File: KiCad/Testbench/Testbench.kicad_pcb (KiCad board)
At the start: 2 copper layers, 119 parts, among them J1 Conn_02x03_Counter_Clockwise, J10 Conn_01x02_Pin, J11 Conn_01x02_Pin, J12 Conn_01x02_Pin, J13 Conn_01x02_Pin, J14 Conn_01x02_Pin, J15 Conn_01x02_Pin, J16 Conn_01x02_Pin, J17 Conn_01x02_Pin, J18 Conn_02x03_Counter_Clockwise, J19 Conn_02x03_Counter_Clockwise, J2 Conn_02x02_Top_Bottom, J20 Conn_02x05_Top_Bottom, J21 Conn_02x02_Top_Bottom, J3 Conn_02x02_Top_Bottom, J4 Conn_02x02_Top_Bottom, J5 Conn_01x01_Pin, J6 Conn_02x05_Counter_Clockwise, J7 Conn_01x02_Pin, J8 Conn_01x02_Pin, J9 Conn_02x05_Counter_Clockwise

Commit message: PCB before first processing
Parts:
- removed the D20 at (111.1, 29.6)
- removed the D21 at (52.2, 62.0)
- removed the D22 at (65.3, 32.4)
- removed the D5 at (139.7, 137.9)
- removed the D6 at (139.8, 144.9)
- removed J5: Conn_01x01_Pin, Connector_Molex:Molex_Mini-Fit_Jr_5566-04A_2x02_P4.20mm_Vertical
- removed the R22 at (111.1, 34.8)
- removed the R23 at (52.2, 57.0)
- removed the R24 at (115.5, 29.4)
- removed R30: R100k, Resistor_SMD:R_1206_3216Metric_Pad1.30x1.75mm_HandSolder
- removed R31: R300, Resistor_SMD:R_1206_3216Metric_Pad1.30x1.75mm_HandSolder
- removed the R6 at (134.8, 102.5)
- removed the R7 at (134.3, 137.9)
- removed the R8 at (134.1, 144.9)
- removed TP44: TestPoint, TestPoint:TestPoint_Keystone_5010-5014_Multipurpose
- added D1: LED, LED_SMD:LED_0805_2012Metric_Pad1.15x1.40mm_HandSolder, B.Cu at (88.1, 67.8)
- added D14: LED, LED_SMD:LED_0805_2012Metric_Pad1.15x1.40mm_HandSolder, B.Cu at (126.7, 105.0)
- added D15: LED, LED_SMD:LED_0805_2012Metric_Pad1.15x1.40mm_HandSolder, B.Cu at (126.5, 145.0)
- added D16: LED, LED_SMD:LED_0805_2012Metric_Pad1.15x1.40mm_HandSolder, B.Cu at (126.7, 95.0)
- added D25: LED, LED_SMD:LED_0805_2012Metric_Pad1.15x1.40mm_HandSolder, B.Cu at (204.8, 33.3)
- added D26: LED, LED_SMD:LED_0805_2012Metric_Pad1.15x1.40mm_HandSolder, B.Cu at (81.5, 35.7)
- added D27: LED, LED_SMD:LED_0805_2012Metric_Pad1.15x1.40mm_HandSolder, B.Cu at (124.3, 35.8)
- added D3: LED, LED_SMD:LED_0805_2012Metric_Pad1.15x1.40mm_HandSolder, B.Cu at (88.3, 75.3)
- added J21: Conn_02x02_Top_Bottom, Connector_Molex:Molex_Mini-Fit_Jr_5566-04A_2x02_P4.20mm_Vertical, F.Cu at (156.6, 46.2)
- added J22: Conn_02x02_Top_Bottom, Connector_Molex:Molex_Mini-Fit_Jr_5566-04A_2x02_P4.20mm_Vertical, F.Cu at (22.7, 48.8)
- added J23: Conn_02x02_Top_Bottom, Connector_Molex:Molex_Mini-Fit_Jr_5566-04A_2x02_P4.20mm_Vertical, F.Cu at (195.7, 45.8)
- added J24: Conn_02x02_Top_Bottom, Connector_Molex:Molex_Mini-Fit_Jr_5566-04A_2x02_P4.20mm_Vertical, F.Cu at (69.5, 21.8)
- added J25: Conn_02x02_Top_Bottom, Connector_Molex:Molex_Mini-Fit_Jr_5566-04A_2x02_P4.20mm_Vertical, F.Cu at (195.7, 21.8)
- added J26: Conn_02x02_Top_Bottom, Connector_Molex:Molex_Mini-Fit_Jr_5566-04A_2x02_P4.20mm_Vertical, F.Cu at (69.5, 48.5)
- added J27: Conn_02x02_Top_Bottom, Connector_Molex:Molex_Mini-Fit_Jr_5566-04A_2x02_P4.20mm_Vertical, F.Cu at (113.2, 21.5)
- added J28: Conn_02x02_Top_Bottom, Connector_Molex:Molex_Mini-Fit_Jr_5566-04A_2x02_P4.20mm_Vertical, F.Cu at (113.3, 46.8)
- added R1: R1k1, Resistor_SMD:R_1206_3216Metric_Pad1.30x1.75mm_HandSolder, B.Cu at (83.3, 67.8)
- added R16: R1k1, Resistor_SMD:R_1206_3216Metric_Pad1.30x1.75mm_HandSolder, B.Cu at (131.4, 105.0)
- added R17: R1k1, Resistor_SMD:R_1206_3216Metric_Pad1.30x1.75mm_HandSolder, B.Cu at (131.3, 145.0)
- added R18: R1k1, Resistor_SMD:R_1206_3216Metric_Pad1.30x1.75mm_HandSolder, B.Cu at (131.4, 95.0)
- added R3: R1k1, Resistor_SMD:R_1206_3216Metric_Pad1.30x1.75mm_HandSolder, B.Cu at (83.5, 75.3)
- added R4: R1k1, Resistor_SMD:R_1206_3216Metric_Pad1.30x1.75mm_HandSolder, B.Cu at (83.6, 79.1)
- D10, D11, D12, D13, D23, D24, D4, D7, D8, D9, R10, R11, R12, R13, R14, R15, R26, R29, R9: moved to B.Cu
- D17: renamed from D14; moved to B.Cu
- D18: renamed from D15; moved to B.Cu
- D19: renamed from D16; moved to B.Cu
- D2: renamed from D1; moved to B.Cu
- D20: renamed from D17; moved to B.Cu
- D21: renamed from D18; moved to B.Cu
- D22: renamed from D19; moved to B.Cu
- D5: renamed from D2; moved to B.Cu
- D6: renamed from D3; moved to B.Cu
- J1: footprint Connector_Molex:Molex_Mini-Fit_Jr_5566-06A_2x03_P4.20mm_Vertical -> Connector_Molex:Molex_Mini-Fit_Jr_5566-08A_2x04_P4.20mm_Vertical
- J19: value Conn_02x03_Counter_Clockwise -> Conn_02x02_Top_Bottom; footprint Connector_Molex:Molex_Mini-Fit_Jr_5566-06A_2x03_P4.20mm_Vertical -> Connector_Molex:Molex_Mini-Fit_Jr_5566-04A_2x02_P4.20mm_Vertical
- J20: value Conn_02x05_Top_Bottom -> Conn_02x02_Top_Bottom; footprint Connector_Molex:Molex_Mini-Fit_Jr_5566-10A_2x05_P4.20mm_Vertical -> Connector_Molex:Molex_Mini-Fit_Jr_5566-04A_2x02_P4.20mm_Vertical
- R19: renamed from R16; moved to B.Cu
- R2: renamed from R1; moved to B.Cu
- R20: renamed from R17; moved to B.Cu
- R21: renamed from R18; moved to B.Cu
- R22: renamed from R19; moved to B.Cu
- R23: renamed from R20; moved to B.Cu
- R24: renamed from R21; moved to B.Cu
- R25, R27, R28: value R100k -> R300; moved to B.Cu
- R5: renamed from R2; moved to B.Cu
- R6: renamed from R3; moved to B.Cu
- R7: renamed from R4; moved to B.Cu
- R8: renamed from R5; moved to B.Cu
- moved J3 166.3 mm to (23.1, 105.5)
- moved J4 154.3 mm to (22.6, 87.5)
- moved D17 146.2 mm to (199.9, 77.5)
- moved R19 146.2 mm to (195.3, 77.5)
- moved D20 146.1 mm to (199.8, 82.0)
- moved R22 146.1 mm to (195.3, 82.0), turned to 0 degrees
- moved R24 146.0 mm to (195.1, 73.5)
- moved D22 146.0 mm to (199.8, 73.5)
- moved TP1 144.5 mm to (34.3, 105.5)
- moved TP3 144.2 mm to (34.3, 111.0)
- moved R7 143.1 mm to (41.3, 108.5)
- moved J18 137.1 mm to (171.6, 81.9)
- moved TP4 130.6 mm to (33.8, 87.5)
- moved TP5 130.5 mm to (33.8, 93.0)
- moved R8 129.4 mm to (40.8, 90.5)
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- renumbered J21 to J29
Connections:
- D10 pad 2: /Shutdown Circuit/1-C4 -> /Shutdown Circuit/1-A1
- D11 pad 2: /Shutdown Circuit/1-E2 -> /Shutdown Circuit/1-B2
- D12 pad 2: /Shutdown Circuit/1-C2 -> /Shutdown Circuit/1-D4
- D13 pad 2: /Shutdown Circuit/1-F1 -> /Shutdown Circuit/1-B4
- D23 pad 1: /Sensors/3-A3 -> /Sensors/3-A2
- D24 pad 1: /Sensors/3-C3 -> /Sensors/2-M4
- D4 pad 1: Net-(D4-K) -> GND-LV_Unfiltered
- D4 pad 2: /Shutdown Circuit/1-A2 -> Net-(D4-A)
- D7 pad 2: /Shutdown Circuit/1-B1 -> /Shutdown Circuit/1-A3
- D8 pad 2: /Shutdown Circuit/1-B3 -> /Shutdown Circuit/1-C1
- D9 pad 2: /Shutdown Circuit/1-E4 -> /Shutdown Circuit/1-D2
- J1 pad 1: /Actuators/2-B4 -> /Actuators/1-G3
- J1 pad 2: /Actuators/2-E4 -> /Actuators/2-C4
- J1 pad 3: /Actuators/1-G3 -> /Actuators/2-D4
- J1 pad 4: GND-LV_Unfiltered -> /Actuators/1-G4
- J1 pad 5: /Actuators/1-G3 -> /Actuators/2-E4
- J1 pad 6: /Actuators/1-G3 -> /Actuators/2-B4
- J19 pad 1: /Sensors/3-A1 -> /Sensors/2-M2
- J19 pad 2: /Sensors/3-B1 -> /Sensors/2-M4
- J19 pad 3: /Sensors/3-A2 -> unconnected-(J19-Pin_3-Pad3)
- J19 pad 4: /Sensors/3-A3 -> /Sensors/2-M3
- J20 pad 1: /Sensors/3-B4 -> /Sensors/3-A1
- J20 pad 2: /Sensors/3-C1 -> /Sensors/3-A2
- J20 pad 3: /Sensors/3-B3 -> unconnected-(J20-Pin_3-Pad3)
- J20 pad 4: /Sensors/2-M2 -> /Sensors/3-B1
- J29 pad 3: unconnected-(J21-Pin_3-Pad3) -> +24V
- J29 pad 4: GND -> GND-LV_Unfiltered
- R2 pad 1: /Actuators/1-G3 -> /Actuators/2-C4
- R25 pad 1: /Sensors/2-M3 -> /Sensors/3-A1
- R25 pad 2: /Sensors/2-M4 -> Net-(D23-A)
- R26 pad 1: /Sensors/3-B4 -> /Sensors/2-M2
- R26 pad 2: Net-(D22-A) (its old number) -> Net-(D24-A)
- R27 pad 1: /Sensors/3-B2 -> /Sensors/3-A4
- R27 pad 2: /Sensors/3-A3 -> Net-(D25-A)
- R28 pad 1: /Sensors/3-C1 -> /Sensors/3-B4
- R28 pad 2: /Sensors/3-B3 -> Net-(D26-A)
- R29 pad 1: /Sensors/3-A4 -> /Sensors/3-C4
- R29 pad 2: Net-(D23-A) -> Net-(D27-A)
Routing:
- net /Shutdown Circuit/1-E1: track 0.00 -> 127.9 mm, vias 0 -> 1
- net /Shutdown Circuit/1-E3: track 0.00 -> 110.9 mm, vias 0 -> 1
- net /Shutdown Circuit/1-D4: track 0.00 -> 94.5 mm, vias 0 -> 1
- net /Shutdown Circuit/1-D2: track 0.00 -> 78.4 mm, vias 0 -> 1
- net /Sensors/3-B4: track 14.8 -> 88.0 mm, vias 0 -> 1
- net /Shutdown Circuit/1-A3: track 5.99 -> 78.3 mm, vias 0 -> 1
- net /Shutdown Circuit/1-A1: track 0.00 -> 69.5 mm, vias 0 -> 1
- net /Sensors/3-A4: track 9.69 -> 73.6 mm, vias 0 -> 1
- net /Shutdown Circuit/1-B2: track 0.00 -> 63.2 mm, vias 0 -> 1
- net /Shutdown Circuit/1-C1: track 0.00 -> 63.0 mm, vias 0 -> 1
- net /Sensors/3-C4: track 15.7 -> 78.7 mm, vias 0 -> 1
- net /Sensors/2-M2: track 24.9 -> 87.6 mm, vias 0 -> 1
- net /Shutdown Circuit/1-B4: track 0.00 -> 61.2 mm, vias 0 -> 1
- net +24V: track 80.6 -> 20.2 mm
- net /Shutdown Circuit/1-C3: track 0.00 -> 58.8 mm, vias 0 -> 1
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- added copper zone on F.Cu, net (none)
- added copper zone on B.Cu, net GND-LV_Unfiltered
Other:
- board outline added: 224 x 186 mm
- board text added: "Actuators"
- board text added: "BP0_SUP"
- board text added: "Brake Pressure 0 (BP0)"
- board text added: "Brake Pressure 0 (BP1)"
- board text added: "Brake Pressure 1 (BP1)"
- board text added: "CAN GND FILTERED GND"
- board text added: "COOLING 1-G3"
- board text added: "COOLING 1-G4"
- board text added: "COOLING 2-C4"
- board text added: "COOLING 2-D4"
- board text added: "External Power"
- board text added: "Inputs"
- board text added: "Mangler: Forket side skal laves på bagsiden Og så skal der laves om på SDC. Sensorkreds. Tjek om forsyning er der. Monter huller til ben."
- board text added: "Outputs"
- board text added: "Power 24VDC"
- board text added: "Power Distribution"
- board text added: "SC.._IN SIGNALS"
- board text added: "SC.._OUT SIGNALS"
- board text added: "SC_BOTS_IN"
- board text added: "SC_Cockpit_IN"
- board text added: "SC_FL_IN"
- board text added: "SC_FR_IN"
- board text added: "SC_Inertia_IN"
- board text added: "SC_Left_IN"
- board text added: "SC_RL_IN"
- board text added: "SC_RR_IN"
- board text added: "SC_Right_IN"
- board text added: "SC_TSMS_IN"
- board text added: "Shutdown Circuit (SDC)"
- board text added: "Steering Wheel"
- board text added: "Unfiltered GND"
- board text removed: "BP0_SUPPLY"
- board text removed: "COOLING"
- board text removed: "GND"
- board text removed: "Mangler: Forket side skal laves på bagsiden Og så skal der laves om på SDC."
- board text removed: "TP1_GND"
- board text removed: "TP1_SIG"
- board text removed: "TP1_SUP"

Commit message: After work 151024
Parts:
- moved R7 38.0 mm to (42.0, 146.6)
- moved R8 38.0 mm to (41.5, 128.6)
- moved J2 38.0 mm to (23.3, 107.5)
- moved J3 38.0 mm to (23.8, 143.5)
- moved J4 38.0 mm to (23.3, 125.5)
- moved TP1 38.0 mm to (35.0, 143.5)
- moved TP2 38.0 mm to (36.5, 107.0)
- moved TP3 38.0 mm to (35.0, 149.0)
- moved TP4 38.0 mm to (34.5, 125.5)
- moved TP5 38.0 mm to (34.5, 131.0)
- moved D17 33.9 mm to (166.6, 70.8)
- moved D18 33.9 mm to (114.7, 75.8)
- moved D19 33.9 mm to (114.8, 70.8)
- moved D21 33.9 mm to (115.0, 65.8)
- moved D22 33.9 mm to (166.5, 66.8)
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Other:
- board size 224 x 186 mm -> 204.2 x 186.5 mm
- board text added: "Steering Wheel (SW)"
- board text removed: "Brake Pressure 0 (BP1)"
- board text removed: "Steering Wheel"

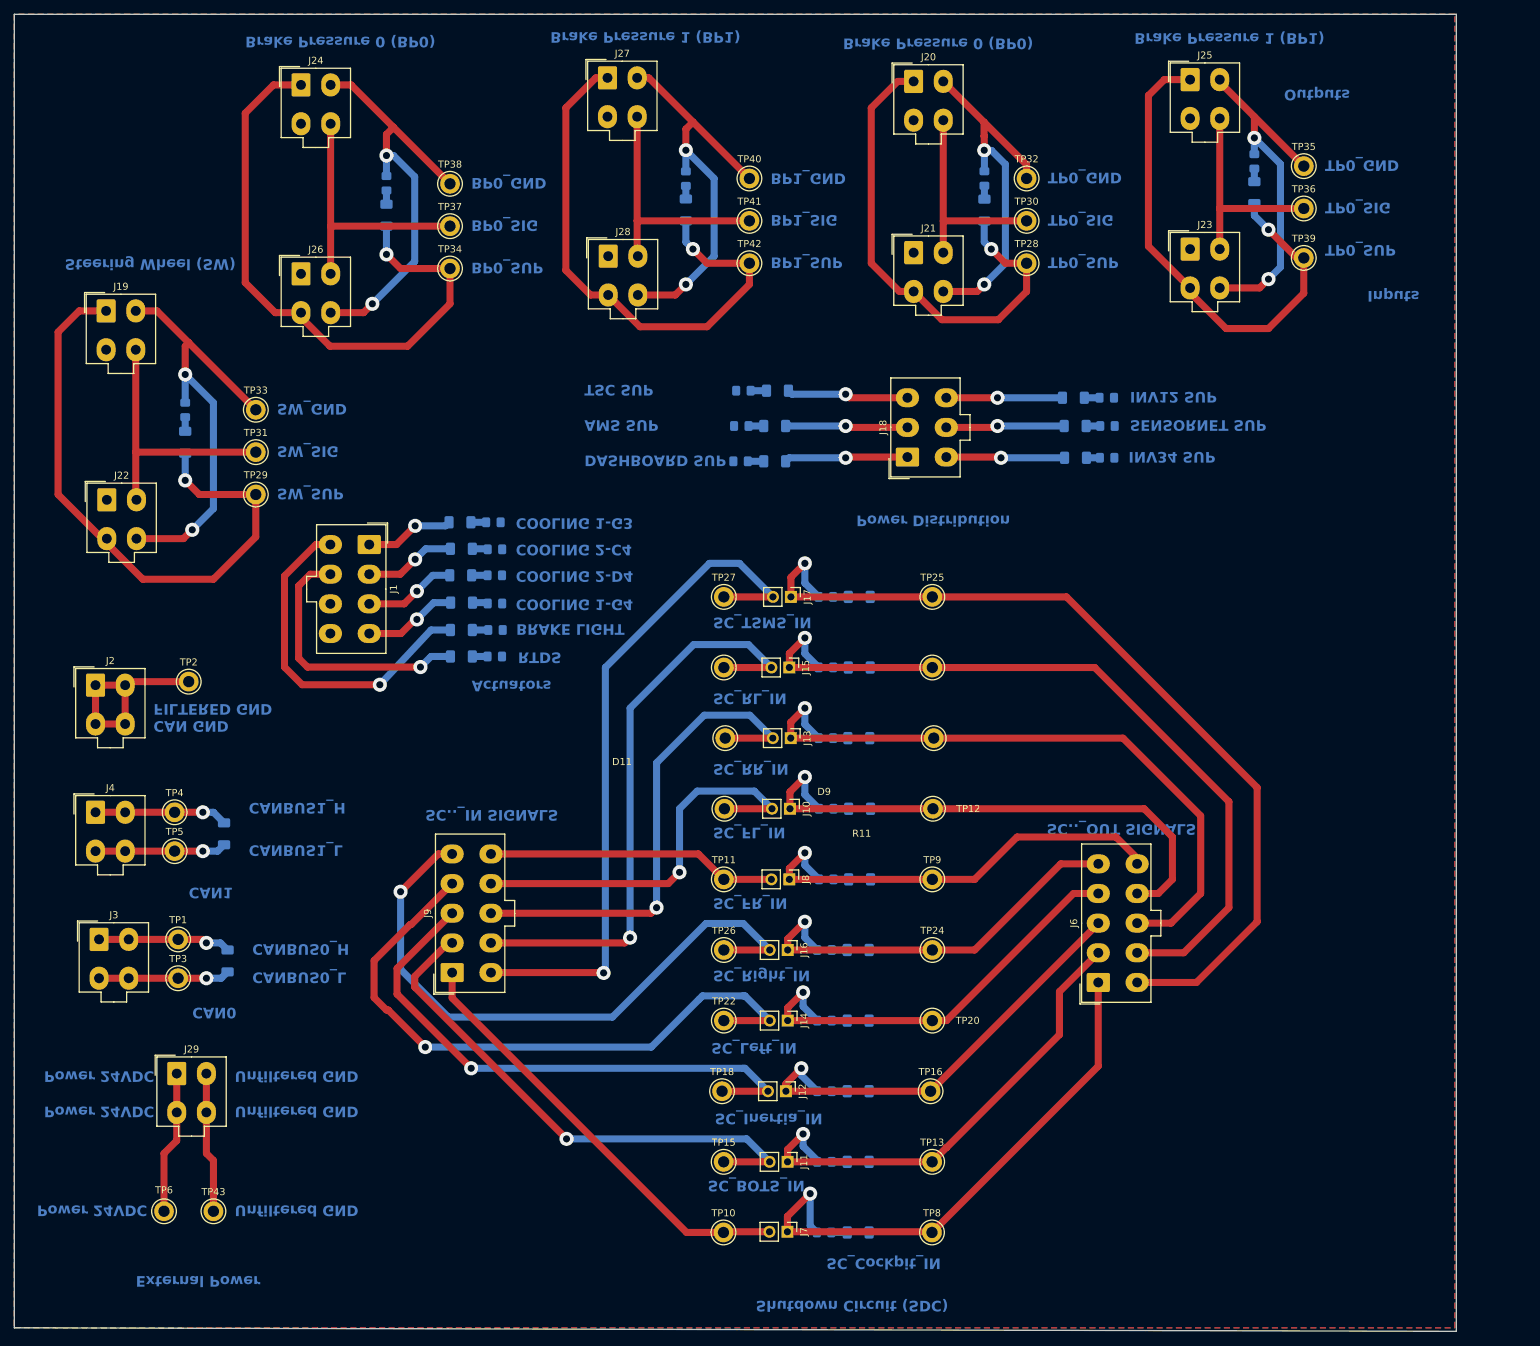
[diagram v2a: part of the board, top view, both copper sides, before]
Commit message: Updated for PCBV2 Updated size and added LED.
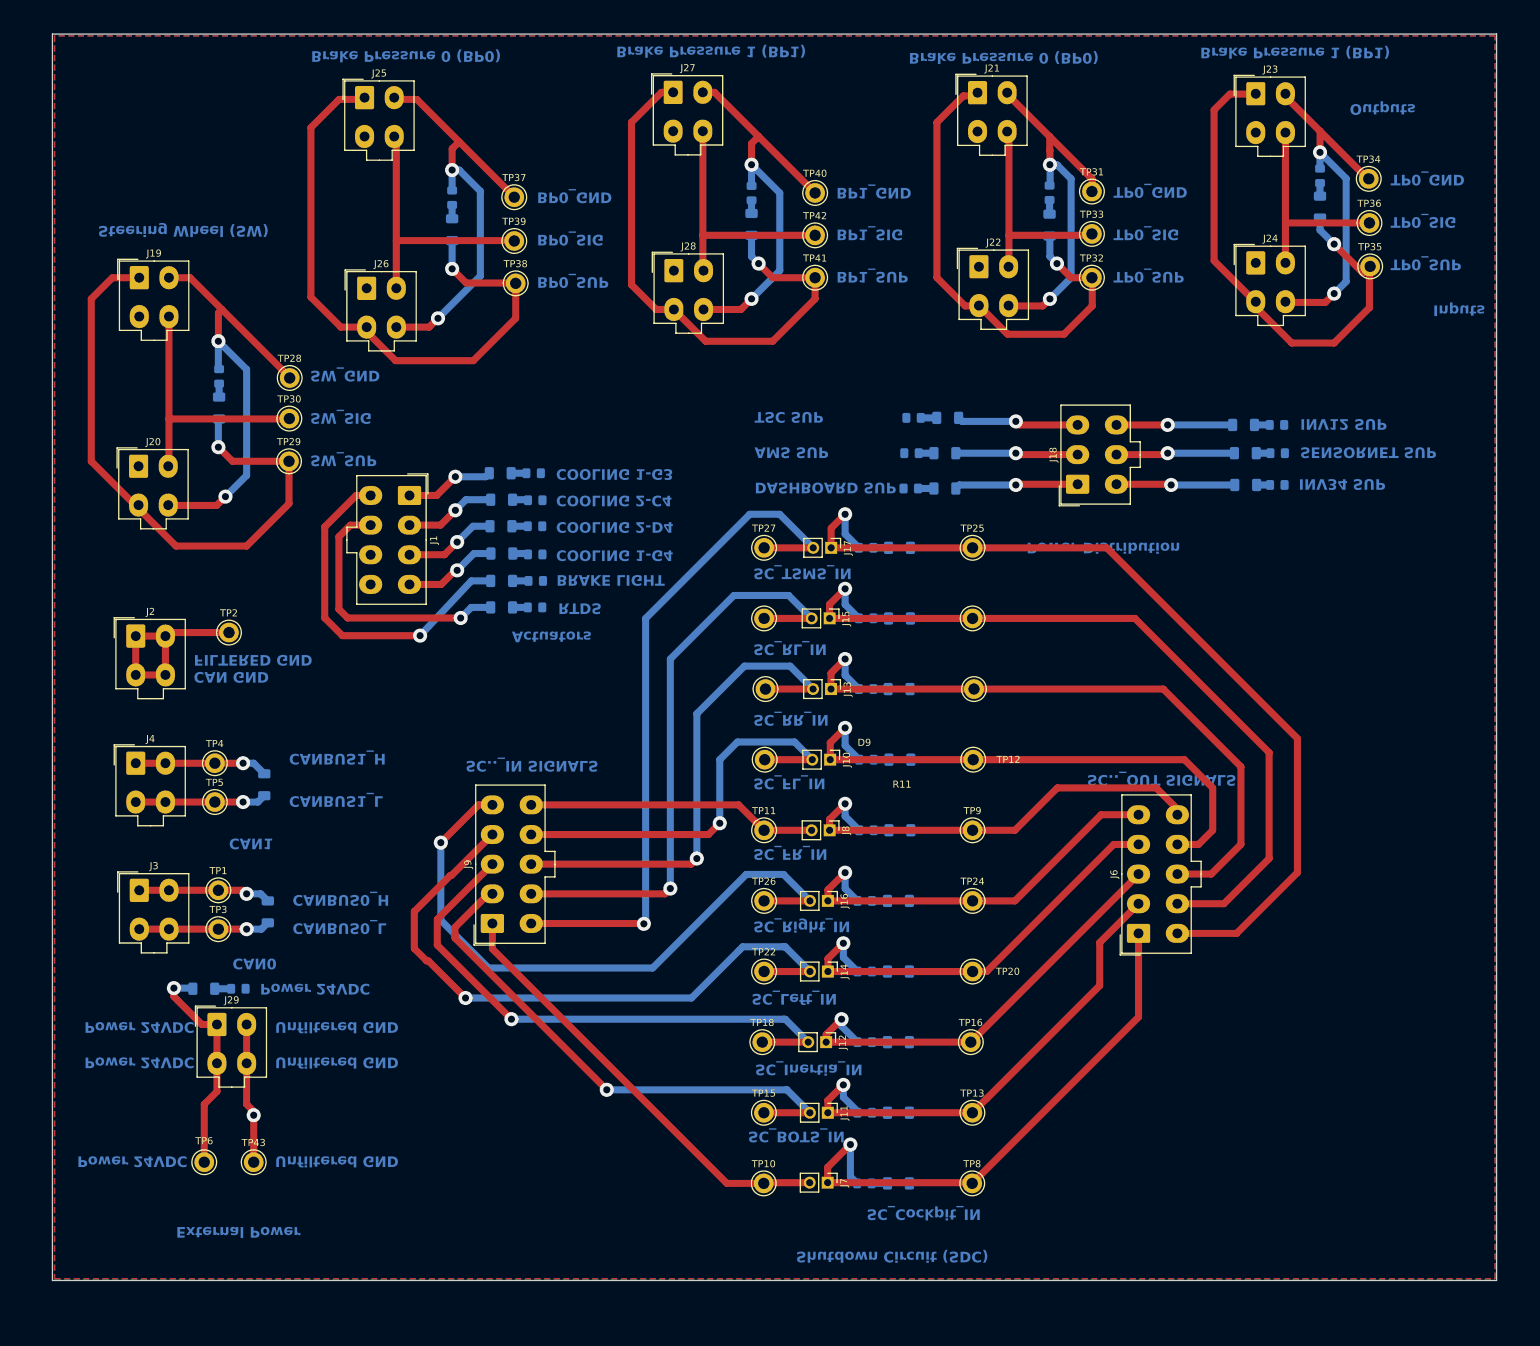
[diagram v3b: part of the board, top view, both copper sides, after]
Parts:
- added D28: LED, LED_SMD:LED_0805_2012Metric_Pad1.15x1.40mm_HandSolder, B.Cu at (43.5, 150.5)
- added R30: R1k1, Resistor_SMD:R_1206_3216Metric_Pad1.30x1.75mm_HandSolder, B.Cu at (38.6, 150.5)
- R19, R20, R21, R22, R23, R24: value R2k1 -> R1k1
- moved J24 137.5 mm to (187.6, 47.7)
- moved TP34 130.7 mm to (203.6, 35.8)
- moved J22 127.8 mm to (148.4, 48.2)
- moved D24 126.2 mm to (158.4, 37.8)
- moved R26 126.2 mm to (158.4, 42.4)
- moved TP31 124.0 mm to (164.4, 37.6)
- moved J20 122.5 mm to (29.4, 76.5)
- moved TP33 121.0 mm to (164.4, 43.6)
- moved J25 116.9 mm to (61.4, 24.3)
- moved D23 111.9 mm to (40.8, 63.8)
- moved R25 111.9 mm to (40.8, 68.2)
- moved TP39 111.8 mm to (82.6, 44.6)
- moved TP30 108.1 mm to (50.8, 69.8)
- moved TP28 105.6 mm to (50.8, 64.0)
- moved R22 24.4 mm to (186.2, 79.2)
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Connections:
- D23 pad 1: /Sensors/3-A2 -> /Sensors/2-M4
- D24 pad 1: /Sensors/2-M4 -> /Sensors/3-A2
- J20 pad 1: /Sensors/3-A1 -> unconnected-(J20-Pin_1-Pad1)
- J20 pad 2: /Sensors/3-A2 -> /Sensors/2-M3
- J20 pad 3: unconnected-(J20-Pin_3-Pad3) -> /Sensors/2-M2
- J20 pad 4: /Sensors/3-B1 -> /Sensors/2-M4
- J21 pad 1: unconnected-(J21-Pin_1-Pad1) -> /Sensors/3-A1
- J21 pad 2: /Sensors/3-B1 -> /Sensors/3-A2
- J21 pad 3: /Sensors/3-A1 -> unconnected-(J21-Pin_3-Pad3)
- J21 pad 4: /Sensors/3-A2 -> /Sensors/3-B1
- J22 pad 2: /Sensors/2-M3 -> /Sensors/3-B1
- J22 pad 3: /Sensors/2-M2 -> /Sensors/3-A1
- J22 pad 4: /Sensors/2-M4 -> /Sensors/3-A2
- J23 pad 1: unconnected-(J23-Pin_1-Pad1) -> /Sensors/3-A4
- J23 pad 2: /Sensors/3-B2 -> /Sensors/3-A3
- J23 pad 3: /Sensors/3-A4 -> unconnected-(J23-Pin_3-Pad3)
- J23 pad 4: /Sensors/3-A3 -> /Sensors/3-B2
- J24 pad 1: /Sensors/3-B4 -> unconnected-(J24-Pin_1-Pad1)
- J24 pad 2: /Sensors/3-B3 -> /Sensors/3-B2
- J24 pad 3: unconnected-(J24-Pin_3-Pad3) -> /Sensors/3-A4
- J24 pad 4: /Sensors/3-C1 -> /Sensors/3-A3
- J25 pad 1: /Sensors/3-A4 -> /Sensors/3-B4
- J25 pad 2: /Sensors/3-A3 -> /Sensors/3-B3
- J25 pad 4: /Sensors/3-B2 -> /Sensors/3-C1
- R25 pad 1: /Sensors/3-A1 -> /Sensors/2-M2
- R26 pad 1: /Sensors/2-M2 -> /Sensors/3-A1
- TP28 pad 1: /Sensors/3-A1 -> /Sensors/2-M4
- TP30 pad 1: /Sensors/3-B1 -> /Sensors/2-M3
- TP31 pad 1: /Sensors/2-M3 -> /Sensors/3-A2
- TP32 pad 1: /Sensors/3-A2 -> /Sensors/3-A1
- TP33 pad 1: /Sensors/2-M4 -> /Sensors/3-B1
- TP34 pad 1: /Sensors/3-B4 -> /Sensors/3-A3
- TP35 pad 1: /Sensors/3-A3 -> /Sensors/3-A4
- TP37 pad 1: /Sensors/3-C1 -> /Sensors/3-B3
- TP38 pad 1: /Sensors/3-B3 -> /Sensors/3-B4
- TP39 pad 1: /Sensors/3-A4 -> /Sensors/3-C1
- TP41 pad 1: /Sensors/3-C2 -> /Sensors/3-C4
- TP42 pad 1: /Sensors/3-C4 -> /Sensors/3-C2
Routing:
- net +24V: track 20.2 -> 31.9 mm, vias 0 -> 1
- net Net-(D28-A): track 0.00 -> 2.32 mm
- net GND-LV_Unfiltered: vias 0 -> 1
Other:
- board size 204.2 x 186.5 mm -> 204.5 x 176.5 mm
